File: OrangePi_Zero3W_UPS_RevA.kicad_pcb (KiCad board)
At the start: 4 copper layers, 65 x 32 mm, 74 parts, among them J1 ORANGE_PI_ZERO_3W_HEADER, J2 BATTERY_1S_PROTECTED_NTC, J3 USB_C_POWER_INPUT, Q1 STL9P3LLH6, SW1 POWER / QON, U1 MAX17048G_T10, U2 BQ25895RTWR, U3 STUSB4500LQTR, U4 USBLC6-2SC6, U5 TPS61088RHLR, U6 TPS259470ARPWR

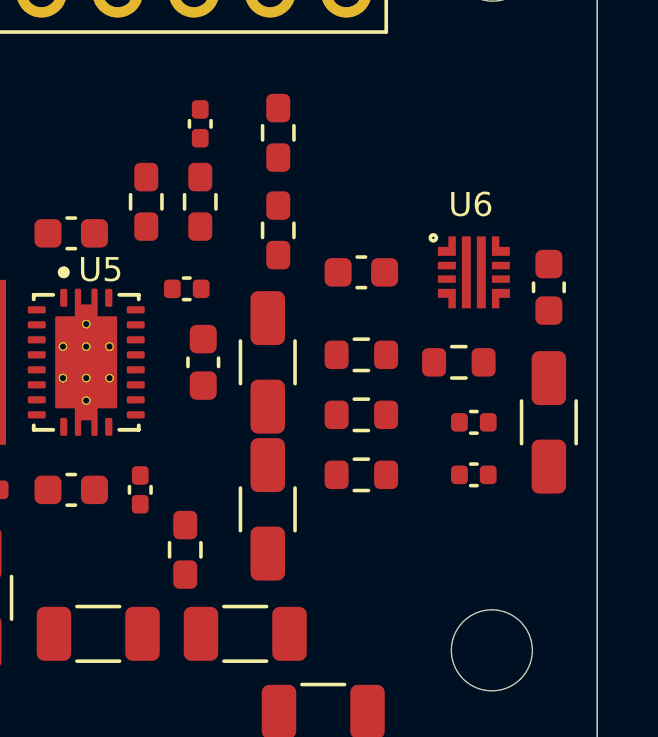
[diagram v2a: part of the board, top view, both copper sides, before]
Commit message: Phase 6B.2B3: optimize TPS25947 output eFuse placement
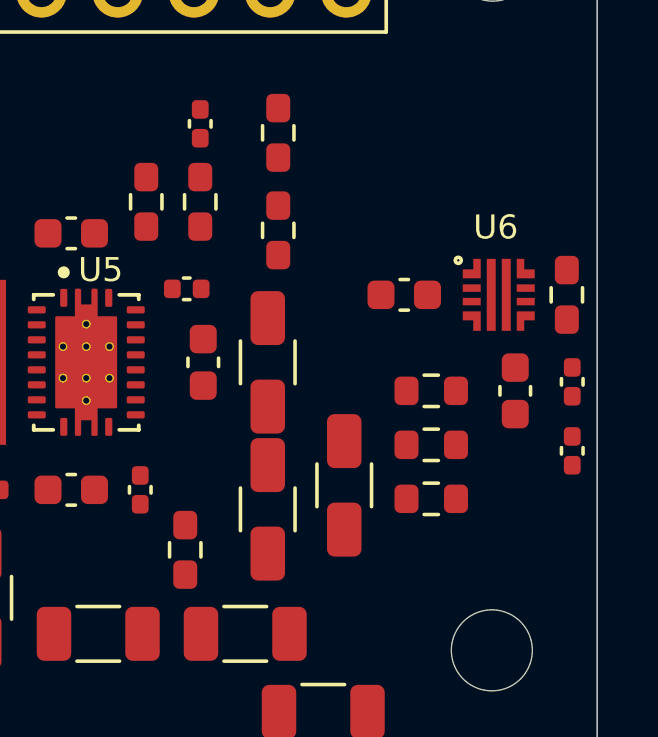
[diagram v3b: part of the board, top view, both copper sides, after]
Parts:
- moved C30 7.14 mm to (112.2, 93.8)
- moved R23 4.25 mm to (119.6, 87.5), turned to 90 degrees
- moved C29 3.63 mm to (117.9, 90.7)
- moved C27 3.55 mm to (119.8, 90.4), turned to 90 degrees
- moved C28 3.38 mm to (119.8, 92.7), turned to 90 degrees
- moved R20 2.62 mm to (115.1, 90.7)
- moved R21 2.54 mm to (115.1, 92.5)
- moved R22 2.46 mm to (115.1, 94.3)
- moved C26 1.61 mm to (114.2, 87.5)
- moved U6 1.12 mm to (117.3, 87.5)
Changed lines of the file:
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@@
 	(footprint "Resistor_SMD:R_0603_1608Metric"
 		(layer "F.Cu")
-		(at 112.77 93.5)
+		(at 115.100 94.300)
 		(descr "Resistor SMD 0603 (1608 Metric), square (rectangular) end terminal, IPC-7351 nominal, (Body size source: IPC-SM-782 page 72, https://www.pcb-3d.com/wordpress/wp-content/uploads/ipc-sm-782a_amendment_1_and_2.pdf), generated with kicad-footprint-generator")
 		(tags "resistor")
@@
 	(footprint "Resistor_SMD:R_0603_1608Metric"
 		(layer "F.Cu")
-		(at 112.77 91.5)
+		(at 115.100 92.500)
 		(descr "Resistor SMD 0603 (1608 Metric), square (rectangular) end terminal, IPC-7351 nominal, (Body size source: IPC-SM-782 page 72, https://www.pcb-3d.com/wordpress/wp-content/uploads/ipc-sm-782a_amendment_1_and_2.pdf), generated with kicad-footprint-generator")
 		(tags "resistor")
@@
 	(footprint "Capacitor_SMD:C_0402_1005Metric"
 		(layer "F.Cu")
-		(at 116.52 91.75)
+		(at 119.800 90.400 90)
 		(descr "Capacitor SMD 0402 (1005 Metric), square (rectangular) end terminal, IPC-7351 nominal, (Body size source: IPC-SM-782 page 76, https://www.pcb-3d.com/wordpress/wp-content/uploads/ipc-sm-782a_amendment_1_and_2.pdf), generated with kicad-footprint-generator")
 		(tags "capacitor")
@@
 	(footprint "Capacitor_SMD:C_1206_3216Metric"
 		(layer "F.Cu")
-		(at 119.02 91.75 90)
+		(at 112.200 93.850 90)
 		(descr "Capacitor SMD 1206 (3216 Metric), square (rectangular) end terminal, IPC-7351 nominal, (Body size source: IPC-SM-782 page 76, https://www.pcb-3d.com/wordpress/wp-content/uploads/ipc-sm-782a_amendment_1_and_2.pdf), generated with kicad-footprint-generator")
 		(tags "capacitor")
@@
 	(footprint "Resistor_SMD:R_0603_1608Metric"
 		(layer "F.Cu")
-		(at 116.02 89.75)
+		(at 119.620 87.500 90)
 		(descr "Resistor SMD 0603 (1608 Metric), square (rectangular) end terminal, IPC-7351 nominal, (Body size source: IPC-SM-782 page 72, https://www.pcb-3d.com/wordpress/wp-content/uploads/ipc-sm-782a_amendment_1_and_2.pdf), generated with kicad-footprint-generator")
 		(tags "resistor")
@@
 	(footprint "Capacitor_SMD:C_0402_1005Metric"
 		(layer "F.Cu")
-		(at 116.52 93.5)
+		(at 119.800 92.700 90)
 		(descr "Capacitor SMD 0402 (1005 Metric), square (rectangular) end terminal, IPC-7351 nominal, (Body size source: IPC-SM-782 page 76, https://www.pcb-3d.com/wordpress/wp-content/uploads/ipc-sm-782a_amendment_1_and_2.pdf), generated with kicad-footprint-generator")
 		(tags "capacitor")
@@
 	(footprint "Resistor_SMD:R_0603_1608Metric"
 		(layer "F.Cu")
-		(at 112.77 89.5)
+		(at 115.100 90.700)
 		(descr "Resistor SMD 0603 (1608 Metric), square (rectangular) end terminal, IPC-7351 nominal, (Body size source: IPC-SM-782 page 72, https://www.pcb-3d.com/wordpress/wp-content/uploads/ipc-sm-782a_amendment_1_and_2.pdf), generated with kicad-footprint-generator")
 		(tags "resistor")
@@
 	(footprint "Capacitor_SMD:C_0603_1608Metric"
 		(layer "F.Cu")
-		(at 119.02 87.25 90)
+		(at 117.900 90.700 90)
 		(descr "Capacitor SMD 0603 (1608 Metric), square (rectangular) end terminal, IPC-7351 nominal, (Body size source: IPC-SM-782 page 76, https://www.pcb-3d.com/wordpress/wp-content/uploads/ipc-sm-782a_amendment_1_and_2.pdf), generated with kicad-footprint-generator")
 		(tags "capacitor")
@@
 	(footprint "TPS25947_fixed:TPS259470ARPWR_RPW0010A"
 		(layer "F.Cu")
-		(at 116.52 86.75)
+		(at 117.350 87.500)
 		(descr "Texas Instruments RPW0010A VQFN-HR-10, 2.0x2.0mm, 0.45mm pitch; corner terminals use duplicate same-number pad primitives to form the recommended L-shaped lands")
 		(tags "TPS25947 RPW0010A VQFN-HR-10 eFuse")
@@
 	(footprint "Capacitor_SMD:C_0603_1608Metric"
 		(layer "F.Cu")
-		(at 112.77 86.75)
+		(at 114.200 87.500)
 		(descr "Capacitor SMD 0603 (1608 Metric), square (rectangular) end terminal, IPC-7351 nominal, (Body size source: IPC-SM-782 page 76, https://www.pcb-3d.com/wordpress/wp-content/uploads/ipc-sm-782a_amendment_1_and_2.pdf), generated with kicad-footprint-generator")
 		(tags "capacitor")

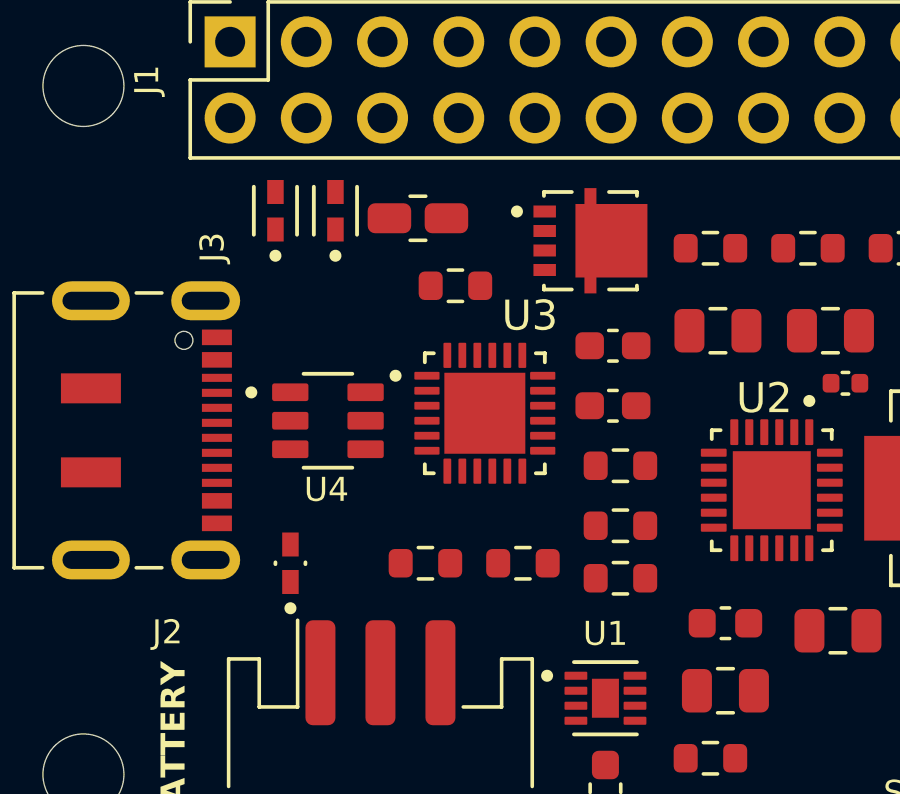
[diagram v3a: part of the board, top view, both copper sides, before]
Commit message: Phase 6B.2B4: optimize USB-C STUSB4500 and ESD placement
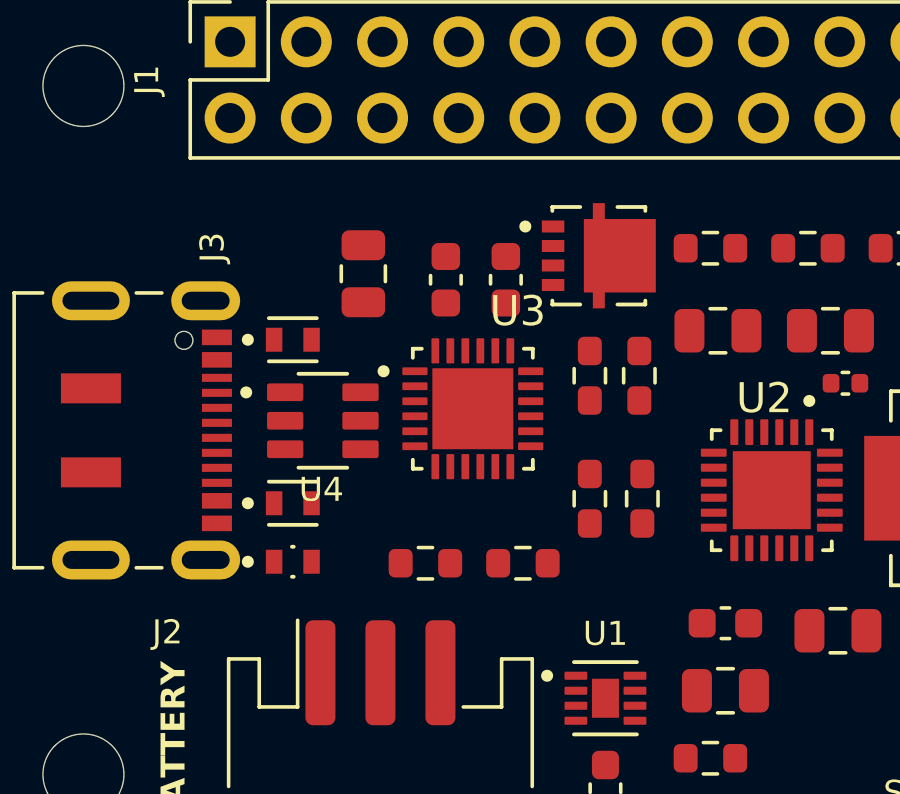
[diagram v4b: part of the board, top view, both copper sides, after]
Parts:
- moved D2 9.85 mm to (66.1, 90.2), turned to 0 degrees
- moved C9 6.98 mm to (71.2, 82.8), turned to 90 degrees
- moved R10 5.39 mm to (76.0, 86.0), turned to -90 degrees
- moved D1 4.34 mm to (66.1, 84.8), turned to 0 degrees
- moved C8 4.19 mm to (73.2, 82.8), turned to 90 degrees
- moved R9 3.07 mm to (77.7, 86.0), turned to -90 degrees
- moved R12 2.75 mm to (77.8, 90.1), turned to 90 degrees
- moved C10 2.60 mm to (68.5, 82.6), turned to 90 degrees
- moved R11 1.36 mm to (76.0, 90.1), turned to 90 degrees
- moved Q1 0.57 mm to (76.3, 82.0)
- moved U3 0.43 mm to (72.1, 87.1)
- moved U4 0.17 mm to (67.1, 87.5)
- moved D3 0.09 mm to (66.1, 92.2), turned to 0 degrees
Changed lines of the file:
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@@
 	(footprint "Capacitor_SMD:C_0603_1608Metric"
 		(layer "F.Cu")
-		(at 76.77 87)
+		(at 71.200 82.800 90)
 		(descr "Capacitor SMD 0603 (1608 Metric), square (rectangular) end terminal, IPC-7351 nominal, (Body size source: IPC-SM-782 page 76, https://www.pcb-3d.com/wordpress/wp-content/uploads/ipc-sm-782a_amendment_1_and_2.pdf), generated with kicad-footprint-generator")
 		(tags "capacitor")
@@
 	(footprint "Capacitor_SMD:C_0805_2012Metric"
 		(layer "F.Cu")
-		(at 70.27 80.75)
+		(at 68.450 82.600 90)
 		(descr "Capacitor SMD 0805 (2012 Metric), square (rectangular) end terminal, IPC-7351 nominal, (Body size source: IPC-SM-782 page 76, https://www.pcb-3d.com/wordpress/wp-content/uploads/ipc-sm-782a_amendment_1_and_2.pdf, https://docs.google.com/spreadsheets/d/1BsfQQcO9C6DZCsRaXUlFlo91Tg2WpOkGARC1WS5S8t0/edit?usp=sharing), generated with kicad-footprint-generator")
 		(tags "capacitor")
@@
 	(footprint "STUSB4500LQTR:QFN50P400X400X100-25N"
 		(layer "F.Cu")
-		(at 72.5 87.25)
+		(at 72.100 87.100)
 		(property "Reference" "U3"
 			(at 1.5 -3.25 0)
@@
 	(footprint "USBLC6-2SC6:SOT95P280X145-6N"
 		(layer "F.Cu")
-		(at 67.27 87.5)
+		(at 67.100 87.500)
 		(property "Reference" "U4"
 			(at -0.05 2.3 0)
@@
 	(footprint "Capacitor_SMD:C_0603_1608Metric"
 		(layer "F.Cu")
-		(at 76.77 85)
+		(at 73.200 82.800 90)
 		(descr "Capacitor SMD 0603 (1608 Metric), square (rectangular) end terminal, IPC-7351 nominal, (Body size source: IPC-SM-782 page 76, https://www.pcb-3d.com/wordpress/wp-content/uploads/ipc-sm-782a_amendment_1_and_2.pdf), generated with kicad-footprint-generator")
 		(tags "capacitor")
@@
 	(footprint "Resistor_SMD:R_0603_1608Metric"
 		(layer "F.Cu")
-		(at 77.02 91)
+		(at 76.000 90.100 90)
 		(descr "Resistor SMD 0603 (1608 Metric), square (rectangular) end terminal, IPC-7351 nominal, (Body size source: IPC-SM-782 page 72, https://www.pcb-3d.com/wordpress/wp-content/uploads/ipc-sm-782a_amendment_1_and_2.pdf), generated with kicad-footprint-generator")
 		(tags "resistor")
@@
 	(footprint "ESDA25P35-1U1M:TVS_ESDA25P35-1U1M"
 		(layer "F.Cu")
-		(at 67.52 80.5 90)
+		(at 66.100 90.250)
 		(property "Reference" "D2"
 			(at -1.8 -0.25 270)
@@
 	(footprint "Resistor_SMD:R_0603_1608Metric"
 		(layer "F.Cu")
-		(at 77.02 92.75)
+		(at 77.750 90.100 90)
 		(descr "Resistor SMD 0603 (1608 Metric), square (rectangular) end terminal, IPC-7351 nominal, (Body size source: IPC-SM-782 page 72, https://www.pcb-3d.com/wordpress/wp-content/uploads/ipc-sm-782a_amendment_1_and_2.pdf), generated with kicad-footprint-generator")
 		(tags "resistor")
@@
 	(footprint "ESDA7P120-1U1M:TVS_ESDA7P120-1U1M"
 		(layer "F.Cu")
-		(at 66.02 92.25 90)
+		(at 66.100 92.200)
 		(property "Reference" "D3"
 			(at 1.75 0 270)
@@
 	(footprint "Resistor_SMD:R_0603_1608Metric"
 		(layer "F.Cu")
-		(at 71.52 83)
+		(at 76.000 86.000 -90)
 		(descr "Resistor SMD 0603 (1608 Metric), square (rectangular) end terminal, IPC-7351 nominal, (Body size source: IPC-SM-782 page 72, https://www.pcb-3d.com/wordpress/wp-content/uploads/ipc-sm-782a_amendment_1_and_2.pdf), generated with kicad-footprint-generator")
 		(tags "resistor")
@@
 	(footprint "STL9P3LLH6:TRANS_STL9P3LLH6"
 		(layer "F.Cu")
-		(at 76.02 81.5)
+		(at 76.300 82.000)
 		(property "Reference" "Q1"
 			(at 0 -2.45 0)
@@
 	(footprint "Resistor_SMD:R_0603_1608Metric"
 		(layer "F.Cu")
-		(at 77.02 89)
+		(at 77.650 86.000 -90)
 		(descr "Resistor SMD 0603 (1608 Metric), square (rectangular) end terminal, IPC-7351 nominal, (Body size source: IPC-SM-782 page 72, https://www.pcb-3d.com/wordpress/wp-content/uploads/ipc-sm-782a_amendment_1_and_2.pdf), generated with kicad-footprint-generator")
 		(tags "resistor")
@@
 	(footprint "ESDA25P35-1U1M:TVS_ESDA25P35-1U1M"
 		(layer "F.Cu")
-		(at 65.52 80.5 90)
+		(at 66.100 84.800)
 		(property "Reference" "D1"
 			(at -1.85 -0.2 270)
